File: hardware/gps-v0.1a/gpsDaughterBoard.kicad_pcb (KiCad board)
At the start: 4 copper layers, 41.4 x 45 mm, 7 parts, among them J1 JST DF12 10P, U1 NEO_M8, U2 BGU7007

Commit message: First Pass routing GPS board
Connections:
- net Net-(J1-Pad4) renamed /RX
- FLT1 pad 1: Net-(FLT1-Pad1) -> Net-(ANT1-Pad1)
- J1 pad 2: Net-(J1-Pad2) -> /TX
- J1 pad 6: Net-(J1-Pad6) -> /PPS
- U1 pad 21: Net-(J1-Pad6) -> /TX
- U1 pad 3: Net-(J1-Pad2) -> /PPS
- U2 pad 3: Net-(U2-Pad3) -> Net-(FLT1-Pad3)
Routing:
- net +3V3: track 0.00 -> 43.8 mm, vias 0 -> 1
- net /PPS: track 0.00 -> 25.8 mm, vias 0 -> 1
- net Net-(ANT1-Pad1): track 0.00 -> 23.8 mm, vias 0 -> 1
- net Net-(J1-Pad10): track 0.00 -> 21.3 mm, vias 0 -> 1
- net /TX: track 0.00 -> 17.9 mm, vias 0 -> 1
- net /RX: track 0.00 -> 16.4 mm, vias 0 -> 1
- net GND: track 0.00 -> 10.3 mm, vias 0 -> 383
- net Net-(U1-Pad11): track 0.00 -> 5.99 mm
- net Net-(FLT1-Pad3): track 0.00 -> 2.04 mm
- added copper zone on F.Cu, net GND
- added copper zone on In1.Cu, net GND

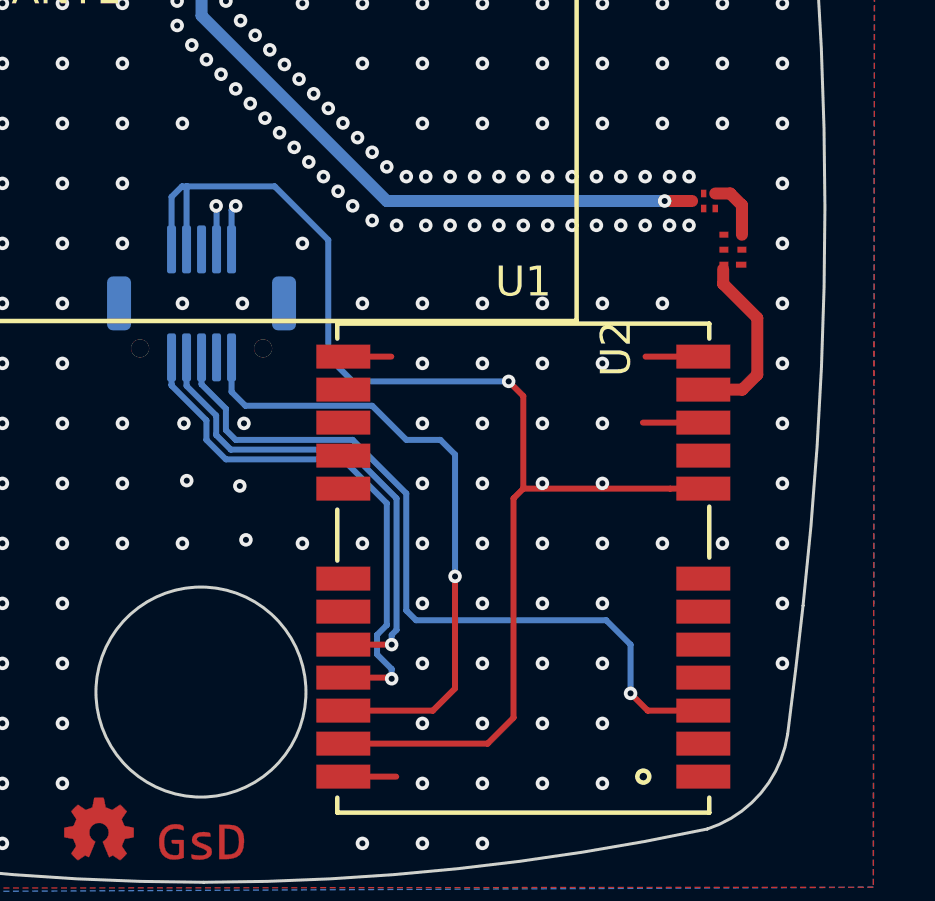
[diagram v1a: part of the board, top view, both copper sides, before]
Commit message: Finished routing the daughterboard.
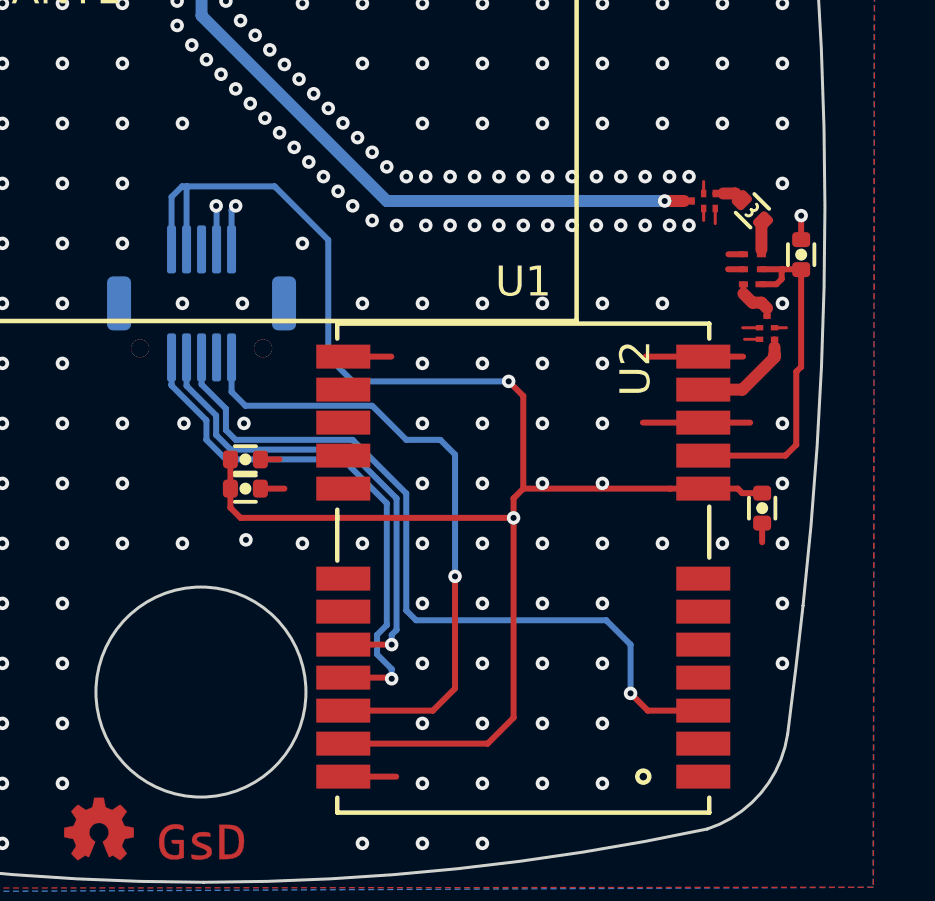
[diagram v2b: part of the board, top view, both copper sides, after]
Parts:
- added C1: 10nF, pkl_dipol:C_0402, F.Cu at (153.0, 124.7)
- added C2: 100nF, pkl_dipol:C_0402, F.Cu at (153.0, 125.7)
- added C3: 100nF, pkl_dipol:C_0402, F.Cu at (170.2, 126.4)
- added C4: 1nF, pkl_dipol:C_0402, F.Cu at (171.5, 117.9)
- added FLT2: SF1186G, gkl_housings_son:SAW-5, F.Cu at (168.2, 116.1)
- added L1: 5.6nH, pkl_dipol:L_0402, F.Cu at (169.9, 116.5)
- moved FLT1 4.72 mm to (170.3, 120.3), turned to 270 degrees
- moved U2 0.92 mm to (169.9, 118.4)
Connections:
- FLT1 pad 1: Net-(ANT1-Pad1) -> Net-(FLT1-Pad1)
- FLT1 pad 2: (no net) -> GND
- FLT1 pad 4: (no net) -> GND
- FLT1 pad 5: (no net) -> GND
- U1 pad 11: Net-(U1-Pad11) -> Net-(FLT1-Pad3)
- U1 pad 9: Net-(U1-Pad9) -> Net-(C4-Pad1)
- U2 pad 1: Net-(U2-Pad1) -> Net-(C4-Pad1)
- U2 pad 2: Net-(U2-Pad2) -> Net-(C4-Pad1)
- U2 pad 3: Net-(FLT1-Pad3) -> Net-(L1-Pad1)
- U2 pad 4: Net-(U2-Pad4) -> GND
- U2 pad 5: Net-(U2-Pad5) -> GND
- U2 pad 6: Net-(U1-Pad11) -> Net-(FLT1-Pad1)
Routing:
- net +3V3: track 43.8 -> 57.0 mm, vias 1 -> 2
- net Net-(C4-Pad1): track 0.00 -> 11.6 mm
- net GND: track 10.3 -> 19.8 mm, vias 383 -> 380
- net Net-(U1-Pad11): track 5.99 -> 0.00 mm
- net Net-(FLT1-Pad1): track 0.00 -> 1.57 mm
- net Net-(FLT1-Pad3): track 2.04 -> 3.42 mm
- net Net-(L1-Pad1): track 0.00 -> 1.12 mm
- net Net-(FLT2-Pad3): track 0.00 -> 0.98 mm

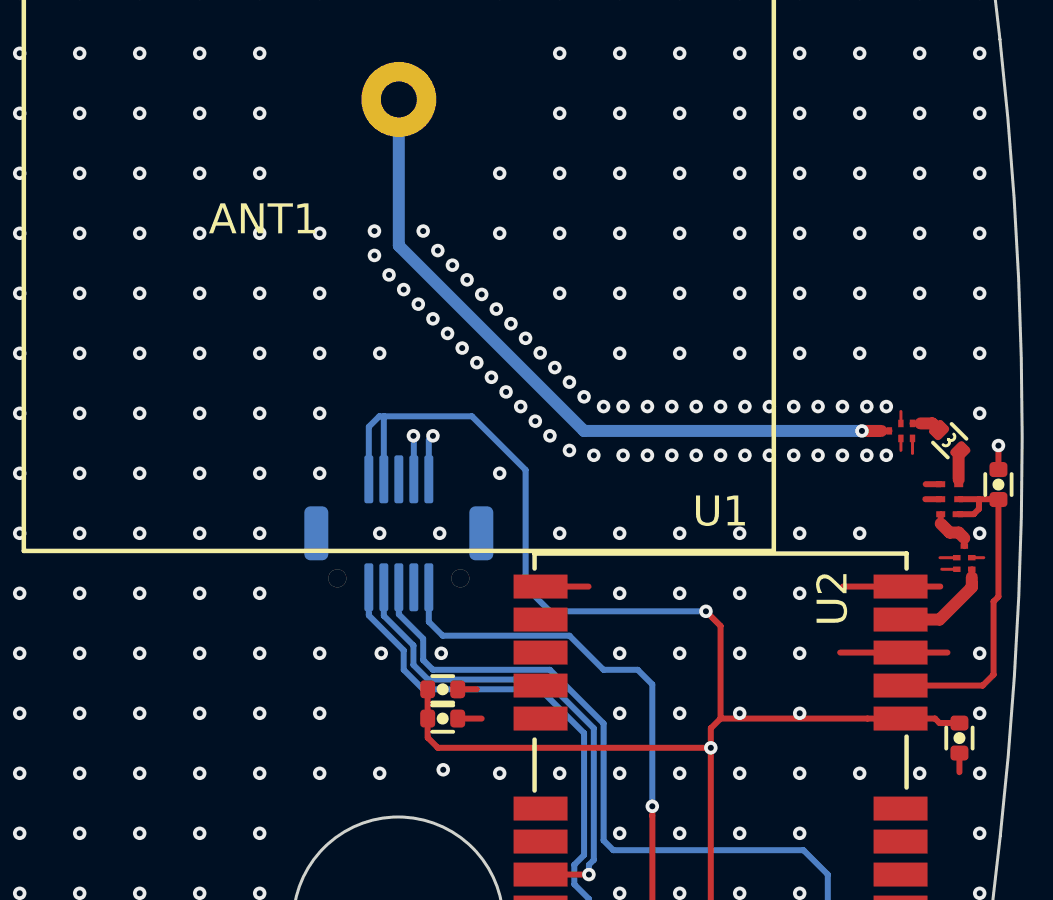
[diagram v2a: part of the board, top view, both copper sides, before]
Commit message: Fixed a DRC error in the GPS PCB. Small layout change to include a logo/product name on the PCB. Created a prototype 'panel' with both PCB attached for production.
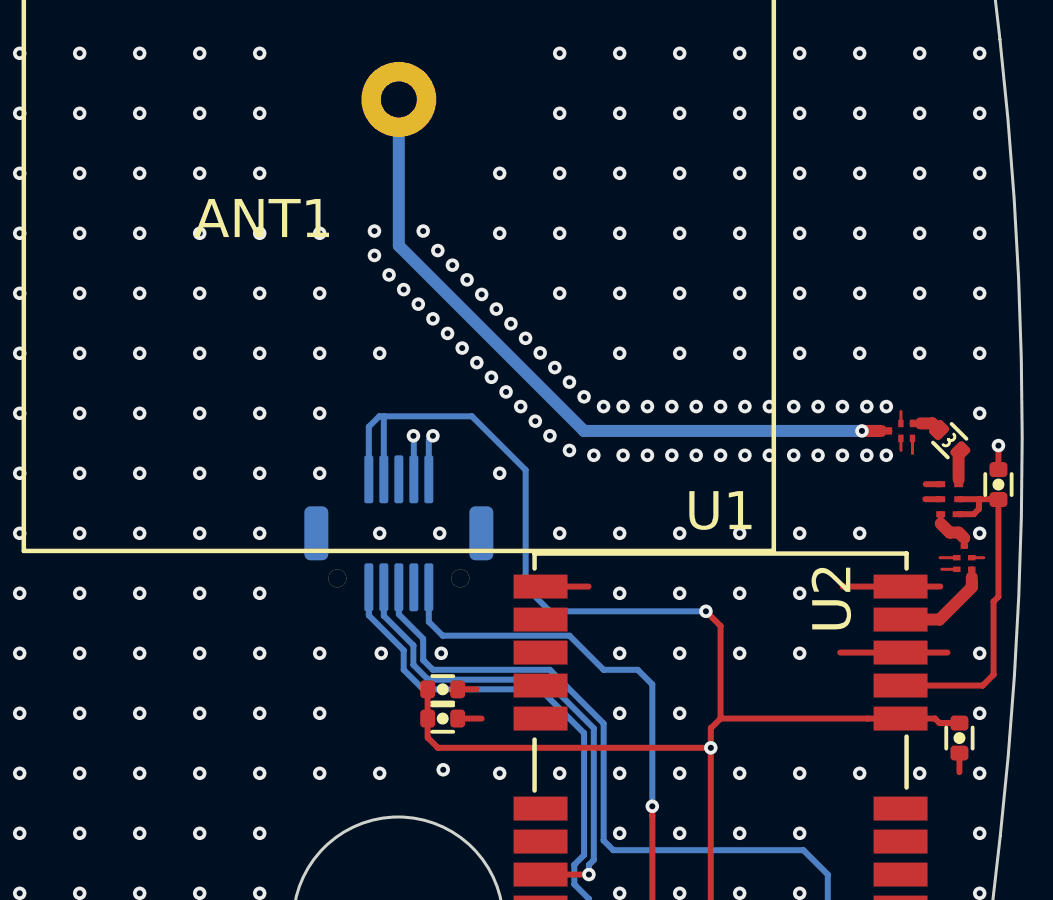
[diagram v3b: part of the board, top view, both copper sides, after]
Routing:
- net GND: vias 380 -> 378
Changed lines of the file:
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@@
     (thickness 1.6)
     (drawings 15)
-    (tracks 516)
+    (tracks 514)
     (zones 0)
     (modules 13)
@@
     (at 151.5 137.575)
     (fp_text reference G*** (at 0 0) (layer F.SilkS) hide
-      (effects (font (size 0.127 0.127) (thickness 0.000001)))
+      (effects (font (size 0 0)))
     )
     (fp_text value LOGO (at 0.75 0) (layer F.SilkS) hide
-      (effects (font (size 0.127 0.127) (thickness 0.000001)))
+      (effects (font (size 0 0)))
     )
     (fp_poly (pts (xy 0.799042 -0.677215) (xy 0.965526 -0.671416) (xy 1.0972 -0.652539) (xy 1.200244 -0.618081)
@@
     (at 148.0875 137.0875)
     (fp_text reference G*** (at 0 0) (layer F.SilkS) hide
-      (effects (font (size 0.127 0.127) (thickness 0.000001)))
+      (effects (font (size 0 0)))
     )
     (fp_text value LOGO (at 0.75 0) (layer F.SilkS) hide
-      (effects (font (size 0.127 0.127) (thickness 0.000001)))
+      (effects (font (size 0 0)))
     )
     (fp_poly (pts (xy 0.034434 -1.070644) (xy 0.067967 -1.070441) (xy 0.094854 -1.070081) (xy 0.115679 -1.069545)
@@
     (at 162.225 128.3125)
     (fp_text reference U1 (at 0 -9.5) (layer F.SilkS)
-      (effects (font (size 1 1) (thickness 0.15)))
+      (effects (font (size 0 0)))
     )
     (fp_text value NEO_M8 (at 0 -10.5) (layer F.Fab)
-      (effects (font (size 1 1) (thickness 0.15)))
+      (effects (font (size 0 0)))
     )
     (fp_line (start 6.2 -8.1) (end 6.2 -7.6) (layer F.SilkS) (width 0.15))
@@
     (at 151.5 105.075 180)
     (fp_text reference ANT1 (at 4.5 -4 180) (layer F.SilkS)
-      (effects (font (size 1 1) (thickness 0.15)))
+      (effects (font (size 0 0)))
     )
     (fp_text value pkl_PATCH_ANTENNA (at 6.5 -2.5 180) (layer F.Fab)
-      (effects (font (size 1 1) (thickness 0.15)))
+      (effects (font (size 0 0)))
     )
     (fp_circle (center 0 0) (end 3 0) (layer F.CrtYd) (width 0.15))
@@
     (at 151.5 119.5375)
     (fp_text reference J1 (at 0.1 0) (layer B.SilkS)
-      (effects (font (size 0.5 0.5) (thickness 0.125)) (justify mirror))
+      (effects (font (size 0 0)) (justify mirror))
     )
     (fp_text value "JST DF12 10P" (at 0 0) (layer B.Fab)
-      (effects (font (size 1 1) (thickness 0.15)) (justify mirror))
+      (effects (font (size 0 0)) (justify mirror))
     )
     (fp_line (start -2.8 1.2) (end -2.8 2.2) (layer B.SilkS) (width 0.2))
@@
     (at 170.35 120.35 270)
     (fp_text reference FLT1 (at 1.1 -2.2 270) (layer F.SilkS) hide
-      (effects (font (size 1 1) (thickness 0.15)))
+      (effects (font (size 0 0)))
     )
     (fp_text value SF1186G (at 1.1 -3.3 270) (layer F.Fab) hide
-      (effects (font (size 1 1) (thickness 0.15)))
+      (effects (font (size 0 0)))
     )
     (pad 1 smd rect (at -0.385 0 270) (size 0.18 0.25) (layers F.Cu F.Paste F.Mask)
@@
     (at 169.8625 118.4 90)
     (fp_text reference U2 (at -3.3 -3.9 90) (layer F.SilkS)
-      (effects (font (size 1 1) (thickness 0.15)))
+      (effects (font (size 0 0)))
     )
     (fp_text value BGU7007 (at -3.3 -4.9 90) (layer F.Fab)
-      (effects (font (size 1 1) (thickness 0.15)))
+      (effects (font (size 0 0)))
     )
     (pad 1 smd rect (at -0.5 0.275 90) (size 0.2 0.35) (layers F.Cu F.Paste F.Mask)
@@
     (attr smd)
     (fp_text reference C1 (at 0 -1.1) (layer F.Fab)
-      (effects (font (size 0.635 0.635) (thickness 0.1)))
+      (effects (font (size 0 0)))
     )
     (fp_text value 10nF (at 0 1.2) (layer F.Fab)
-      (effects (font (size 0.635 0.635) (thickness 0.1)))
+      (effects (font (size 0 0)))
     )
     (fp_circle (center 0 0) (end 0.1 0) (layer F.SilkS) (width 0.2))
@@
     (attr smd)
     (fp_text reference C2 (at 0 -1.1) (layer F.Fab)
-      (effects (font (size 0.635 0.635) (thickness 0.1)))
+      (effects (font (size 0 0)))
     )
     (fp_text value 100nF (at 0 1.2) (layer F.Fab)
-      (effects (font (size 0.635 0.635) (thickness 0.1)))
+      (effects (font (size 0 0)))
     )
     (fp_line (start 0.35 0.44) (end -0.35 0.44) (layer F.SilkS) (width 0.13))
@@
     (attr smd)
     (fp_text reference C3 (at 0 -1.1 270) (layer F.Fab)
-      (effects (font (size 0.635 0.635) (thickness 0.1)))
+      (effects (font (size 0 0)))
     )
     (fp_text value 100nF (at 0 1.2 270) (layer F.Fab)
-      (effects (font (size 0.635 0.635) (thickness 0.1)))
+      (effects (font (size 0 0)))
     )
     (fp_circle (center 0 0) (end 0.1 0) (layer F.SilkS) (width 0.2))
@@
     (attr smd)
     (fp_text reference C4 (at 0 -1.1 90) (layer F.Fab)
-      (effects (font (size 0.635 0.635) (thickness 0.1)))
+      (effects (font (size 0 0)))
     )
     (fp_text value 1nF (at 0 1.2 90) (layer F.Fab)
-      (effects (font (size 0.635 0.635) (thickness 0.1)))
+      (effects (font (size 0 0)))
     )
     (fp_line (start 0.35 0.44) (end -0.35 0.44) (layer F.SilkS) (width 0.13))
@@
     (at 168.2375 116.125)
     (fp_text reference FLT2 (at 1.1 -2.2) (layer F.SilkS) hide
-      (effects (font (size 1 1) (thickness 0.15)))
+      (effects (font (size 0 0)))
     )
     (fp_text value SF1186G (at 1.1 -3.3) (layer F.Fab) hide
-      (effects (font (size 1 1) (thickness 0.15)))
+      (effects (font (size 0 0)))
     )
     (pad 1 smd rect (at -0.385 0) (size 0.18 0.25) (layers F.Cu F.Paste F.Mask)
@@
     (attr smd)
     (fp_text reference L1 (at 0 -1.1 135) (layer F.Fab)
-      (effects (font (size 0.635 0.635) (thickness 0.1)))
+      (effects (font (size 0 0)))
     )
     (fp_text value 5.6nH (at 0 1.2 135) (layer F.Fab)
-      (effects (font (size 0.635 0.635) (thickness 0.1)))
+      (effects (font (size 0 0)))
     )
     (fp_arc (start 0.06 -0.125) (end 0.06 0) (angle 180) (layer F.SilkS) (width 0.1))
@@
     (fp_line (start -0.35 -0.44) (end 0.35 -0.44) (layer F.SilkS) (width 0.13))
     (fp_line (start 0.35 0.44) (end -0.35 0.44) (layer F.SilkS) (width 0.13))
-    (pad 1 smd roundrect (at -0.5 0 135) (size 0.5 0.6) (layers F.Cu F.Paste F.Mask) (roundrect_rratio 0.25)
+    (pad 1 smd roundrect (at -0.499999 0 135) (size 0.5 0.6) (layers F.Cu F.Paste F.Mask) (roundrect_rratio 0.25)
       (net 26 "Net-(L1-Pad1)"))
-    (pad 2 smd roundrect (at 0.5 0 135) (size 0.5 0.6) (layers F.Cu F.Paste F.Mask) (roundrect_rratio 0.25)
+    (pad 2 smd roundrect (at 0.499999 0 135) (size 0.5 0.6) (layers F.Cu F.Paste F.Mask) (roundrect_rratio 0.25)
       (net 25 "Net-(FLT2-Pad3)"))
     (model ${KISYS3DMOD}/Inductor_SMD.3dshapes/L_0402_1005Metric.step
@@
   (via (at 158.8625 137.5375) (size 0.45) (drill 0.2) (layers F.Cu B.Cu) (net 1))
   (via (at 160.8625 137.5375) (size 0.45) (drill 0.2) (layers F.Cu B.Cu) (net 1))
-  (via (at 164.8625 125.5375) (size 0.45) (drill 0.2) (layers F.Cu B.Cu) (net 1))
-  (via (at 162.8625 125.5375) (size 0.45) (drill 0.2) (layers F.Cu B.Cu) (net 1))
   (via (at 152.91401 123.5375) (size 0.45) (drill 0.2) (layers F.Cu B.Cu) (net 1))
   (via (at 154.8625 127.5375) (size 0.45) (drill 0.2) (layers F.Cu B.Cu) (net 1))

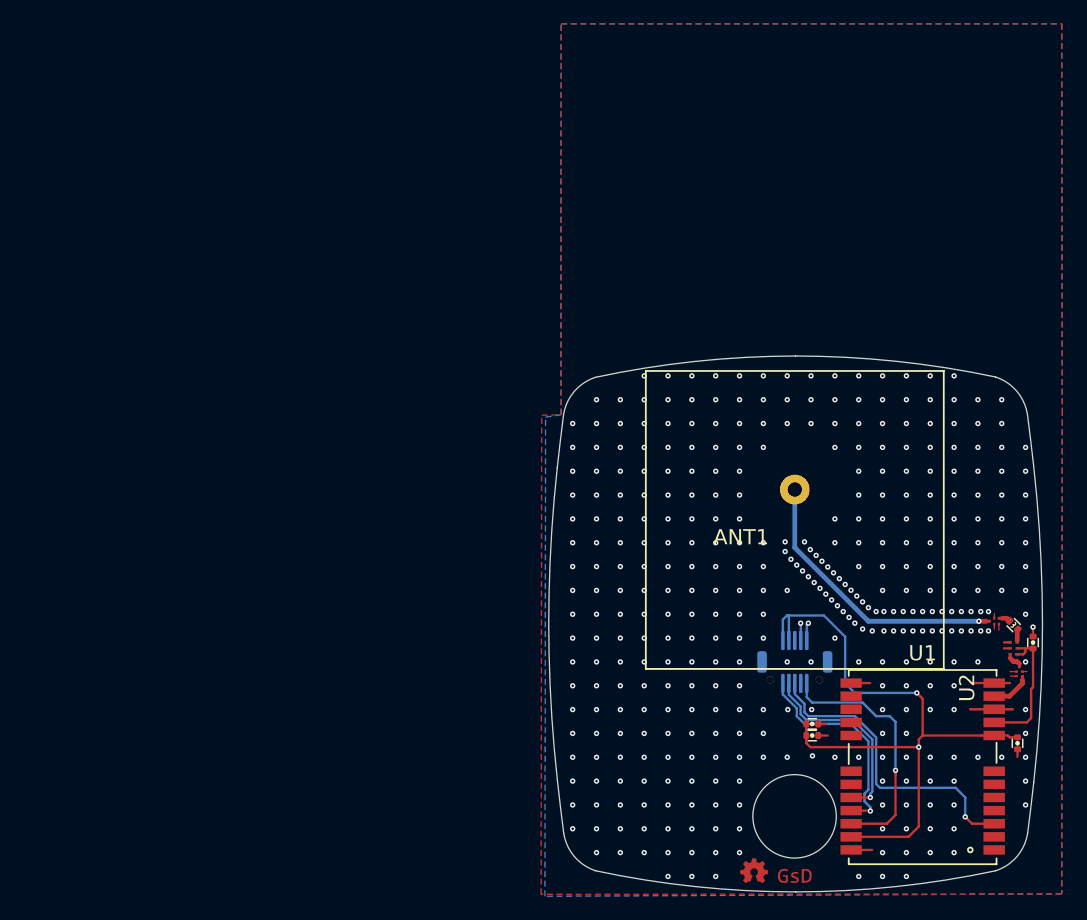
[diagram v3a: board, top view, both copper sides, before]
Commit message: Updated GPS pcb with impoved RF path, and potetially easier to solder filters. Added USB connector to GPS pcb for debugging ublox.
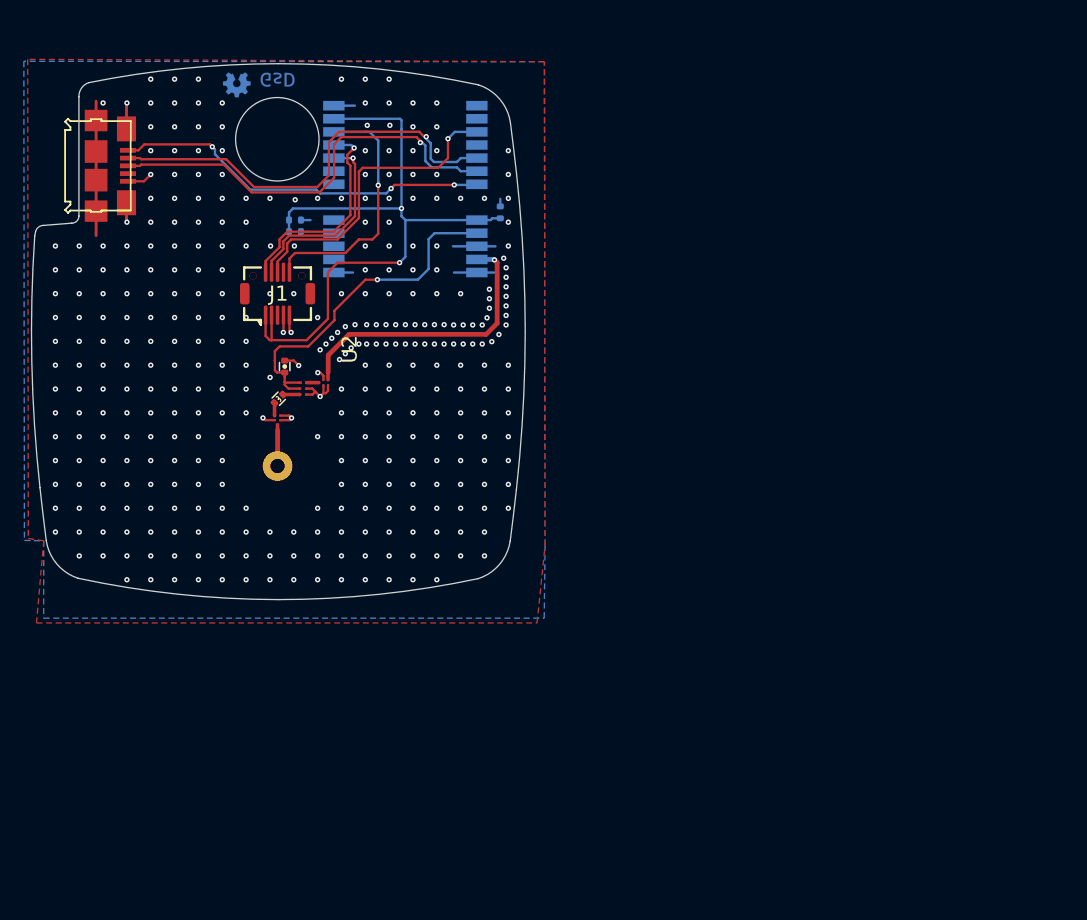
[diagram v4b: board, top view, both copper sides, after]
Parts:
- added G***: LOGO, LOGO, B.Cu at (98.6, 86.7)
- added J2: USB_OTG, Connector_USB_Micro_B_SMD, F.Cu at (92.9, 77.9)
- ANT1, C1, C2, C3, G*** (x2), U1: moved to B.Cu
- J1: moved to F.Cu
- moved G*** 79.8 mm to (108.1, 70.6)
- moved G*** 79.0 mm to (104.7, 71.1)
- moved C4 66.9 mm to (108.7, 94.8)
- moved U1 65.0 mm to (118.8, 79.9)
- moved L1 64.5 mm to (108.2, 97.5), turned to 225 degrees
- moved U2 63.5 mm to (110.2, 96.6), turned to 270 degrees
- moved FLT1 63.2 mm to (112.0, 96.1), turned to 0 degrees
- moved FLT2 62.5 mm to (108.1, 99.3), turned to 90 degrees
- moved C3 62.2 mm to (126.8, 81.8), turned to 90 degrees
- moved C2 61.3 mm to (109.6, 82.5)
- moved C1 59.9 mm to (109.6, 83.4)
- moved J1 53.3 mm to (108.1, 88.6)
- moved ANT1 43.4 mm to (108.1, 103.1)
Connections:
- U1 pad 5: Net-(U1-Pad5) -> /DATA_N
- U1 pad 6: Net-(U1-Pad6) -> /DATA_P
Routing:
- net /DATA_N: track 0.00 -> 35.9 mm, vias 0 -> 1
- net /DATA_P: track 0.00 -> 35.9 mm, vias 0 -> 1
- net Net-(J2-Pad1): track 0.00 -> 31.7 mm, vias 0 -> 3
- net GND: track 19.8 -> 42.1 mm, vias 378 -> 356
- net Net-(FLT1-Pad3): track 3.42 -> 24.2 mm, vias 0 -> 1
- net Net-(ANT1-Pad1): track 23.8 -> 3.47 mm, vias 1 -> 0
- net Net-(C4-Pad1): track 11.6 -> 29.2 mm, vias 0 -> 1
- net Net-(FLT1-Pad1): track 1.57 -> 1.02 mm
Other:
- outline, holes or cut-outs redrawn
